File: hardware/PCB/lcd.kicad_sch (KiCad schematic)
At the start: 0 parts

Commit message: Schematic: Create lcd symbol and add to schematic
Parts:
- added DS1: CH430WQ12A-T, symbol CustomSymbols:Adafruit_TFT_480x272_Touchscreen
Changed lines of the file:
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@@
 	(generator_version "9.0")
 	(paper "A4")
+	(symbol
+		(lib_id "CustomSymbols:Adafruit_TFT_480x272_Touchscreen")
+		(at 177.8 96.52 0)
+		(unit 1)
+		(exclude_from_sim no)
+		(in_bom yes)
+		(on_board yes)
+		(dnp no)
+		(fields_autoplaced yes)
+		(property "Reference" "DS1"
+			(at 186.055 94.0378 0)
+			(effects
+				(font
+					(size 1.27 1.27)
+				)
+				(justify left)
+			)
+		)
+		(property "Value" "CH430WQ12A-T"
+			(at 186.055 96.4621 0)
+			(effects
+				(font
+					(size 1.27 1.27)
+				)
+				(justify left)
+			)
+		)
+		(property "Footprint" ""
+			(at 177.8 96.52 0)
+			(effects
+				(font
+					(size 1.27 1.27)
+				)
+				(hide yes)
+			)
+		)
+		(property "Datasheet" "https://cdn-shop.adafruit.com/product-files/1591/CH430WQ12A-T+display+diagram.png"
+			(at 181.102 152.4 0)
+			(effects
+				(font
+					(size 1.27 1.27)
+				)
+				(hide yes)
+			)
+		)
+		(property "Description" ""
+			(at 177.8 96.52 0)
+			(effects
+				(font
+					(size 1.27 1.27)
+				)
+				(hide yes)
+			)
+		)
+		(pin "8"
+		)
+		(pin "22"
+		)
+		(pin "24"
+		)
+		(pin "26"
+		)
+		(pin "9"
+		)
+		(pin "29"
+		)
+		(pin "31"
+		)
+		(pin "5"
+		)
+		(pin "12"
+		)
+		(pin "14"
+		)
+		(pin "19"
+		)
+		(pin "15"
+		)
+		(pin "3"
+		)
+		(pin "21"
+		)
+		(pin "11"
+		)
+		(pin "13"
+		)
+		(pin "4"
+		)
+		(pin "10"
+		)
+		(pin "18"
+		)
+		(pin "1"
+		)
+		(pin "6"
+		)
+		(pin "16"
+		)
+		(pin "17"
+		)
+		(pin "2"
+		)
+		(pin "7"
+		)
+		(pin "20"
+		)
+		(pin "23"
+		)
+		(pin "25"
+		)
+		(pin "27"
+		)
+		(pin "28"
+		)
+		(pin "30"
+		)
+		(pin "33"
+		)
+		(pin "38"
+		)
+		(pin "32"
+		)
+		(pin "34"
+		)
+		(pin "35"
+		)
+		(pin "40"
+		)
+		(pin "37"
+		)
+		(pin "39"
+		)
+		(pin "36"
+		)
+		(instances
+			(project ""
+				(path "/2826ff7c-9767-4078-8ea2-1cd3a432abf3/e982bc10-c57a-42ac-b92d-a536dd69a0fd"
+					(reference "DS1")
+					(unit 1)
+				)
+			)
+		)
+	)
 )

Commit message: Missing changes in last commit
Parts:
- added U1: TSC2013QRSARQ1, Package_DFN_QFN:Texas_RSA_VQFN-16-1EP_4x4mm_P0.65mm_EP2.7x2.7mm, symbol CustomSymbols:TSC2013QRSARQ1
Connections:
- net at DS1.37 (XR): now also U1.11 (X+)
- net at DS1.38 (YD): now also U1.12 (Y+)
- net at DS1.39 (XL): now also U1.13 (X-)
- net at DS1.40 (YU): now also U1.14 (Y-)
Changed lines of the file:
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@@
 	(generator_version "9.0")
 	(paper "A4")
+	(wire
+		(pts
+			(xy 127 137.16) (xy 175.26 137.16)
+		)
+		(stroke
+			(width 0)
+			(type default)
+		)
+	)
+	(wire
+		(pts
+			(xy 127 144.78) (xy 175.26 144.78)
+		)
+		(stroke
+			(width 0)
+			(type default)
+		)
+	)
+	(wire
+		(pts
+			(xy 127 142.24) (xy 175.26 142.24)
+		)
+		(stroke
+			(width 0)
+			(type default)
+		)
+	)
+	(wire
+		(pts
+			(xy 127 139.7) (xy 175.26 139.7)
+		)
+		(stroke
+			(width 0)
+			(type default)
+		)
+	)
+	(symbol
+		(lib_id "CustomSymbols:TSC2013QRSARQ1")
+		(at 109.22 193.04 0)
+		(unit 1)
+		(exclude_from_sim no)
+		(in_bom yes)
+		(on_board yes)
+		(dnp no)
+		(fields_autoplaced yes)
+		(property "Reference" "U1"
+			(at 111.3633 124.46 0)
+			(effects
+				(font
+					(size 1.27 1.27)
+				)
+				(justify left)
+			)
+		)
+		(property "Value" "TSC2013QRSARQ1"
+			(at 111.3633 127 0)
+			(effects
+				(font
+					(size 1.27 1.27)
+				)
+				(justify left)
+			)
+		)
+		(property "Footprint" "Package_DFN_QFN:Texas_RSA_VQFN-16-1EP_4x4mm_P0.65mm_EP2.7x2.7mm"
+			(at 109.22 193.04 0)
+			(effects
+				(font
+					(size 1.27 1.27)
+				)
+				(hide yes)
+			)
+		)
+		(property "Datasheet" "https://www.ti.com/lit/ds/symlink/tsc2013-q1.pdf?HQS=dis-dk-null-digikeymode-dsf-pf-null-wwe&ts=1768864921231&ref_url=https%253A%252F%252Fwww.ti.com%252Fgeneral%252Fdocs%252Fsuppproductinfo.tsp%253FdistId%253D10%2526gotoUrl%253Dhttps%253A%252F%252Fwww.ti.com%252Flit%252Fgpn%252Ftsc2013-q1"
+			(at 109.22 193.04 0)
+			(effects
+				(font
+					(size 1.27 1.27)
+				)
+				(hide yes)
+			)
+		)
+		(property "Description" "Resistive Touchscreen Driver IC"
+			(at 109.22 193.04 0)
+			(effects
+				(font
+					(size 1.27 1.27)
+				)
+				(hide yes)
+			)
+		)
+		(pin "16"
+		)
+		(pin "3"
+		)
+		(pin "5"
+		)
+		(pin "1"
+		)
+		(pin "7"
+		)
+		(pin "6"
+		)
+		(pin "2"
+		)
+		(pin "10"
+		)
+		(pin "4"
+		)
+		(pin "13"
+		)
+		(pin "8"
+		)
+		(pin "12"
+		)
+		(pin "14"
+		)
+		(pin "15"
+		)
+		(pin "9"
+		)
+		(pin "11"
+		)
+		(instances
+			(project ""
+				(path "/2826ff7c-9767-4078-8ea2-1cd3a432abf3/e982bc10-c57a-42ac-b92d-a536dd69a0fd"
+					(reference "U1")
+					(unit 1)
+				)
+			)
+		)
+	)
 	(symbol
 		(lib_id "CustomSymbols:Adafruit_TFT_480x272_Touchscreen")

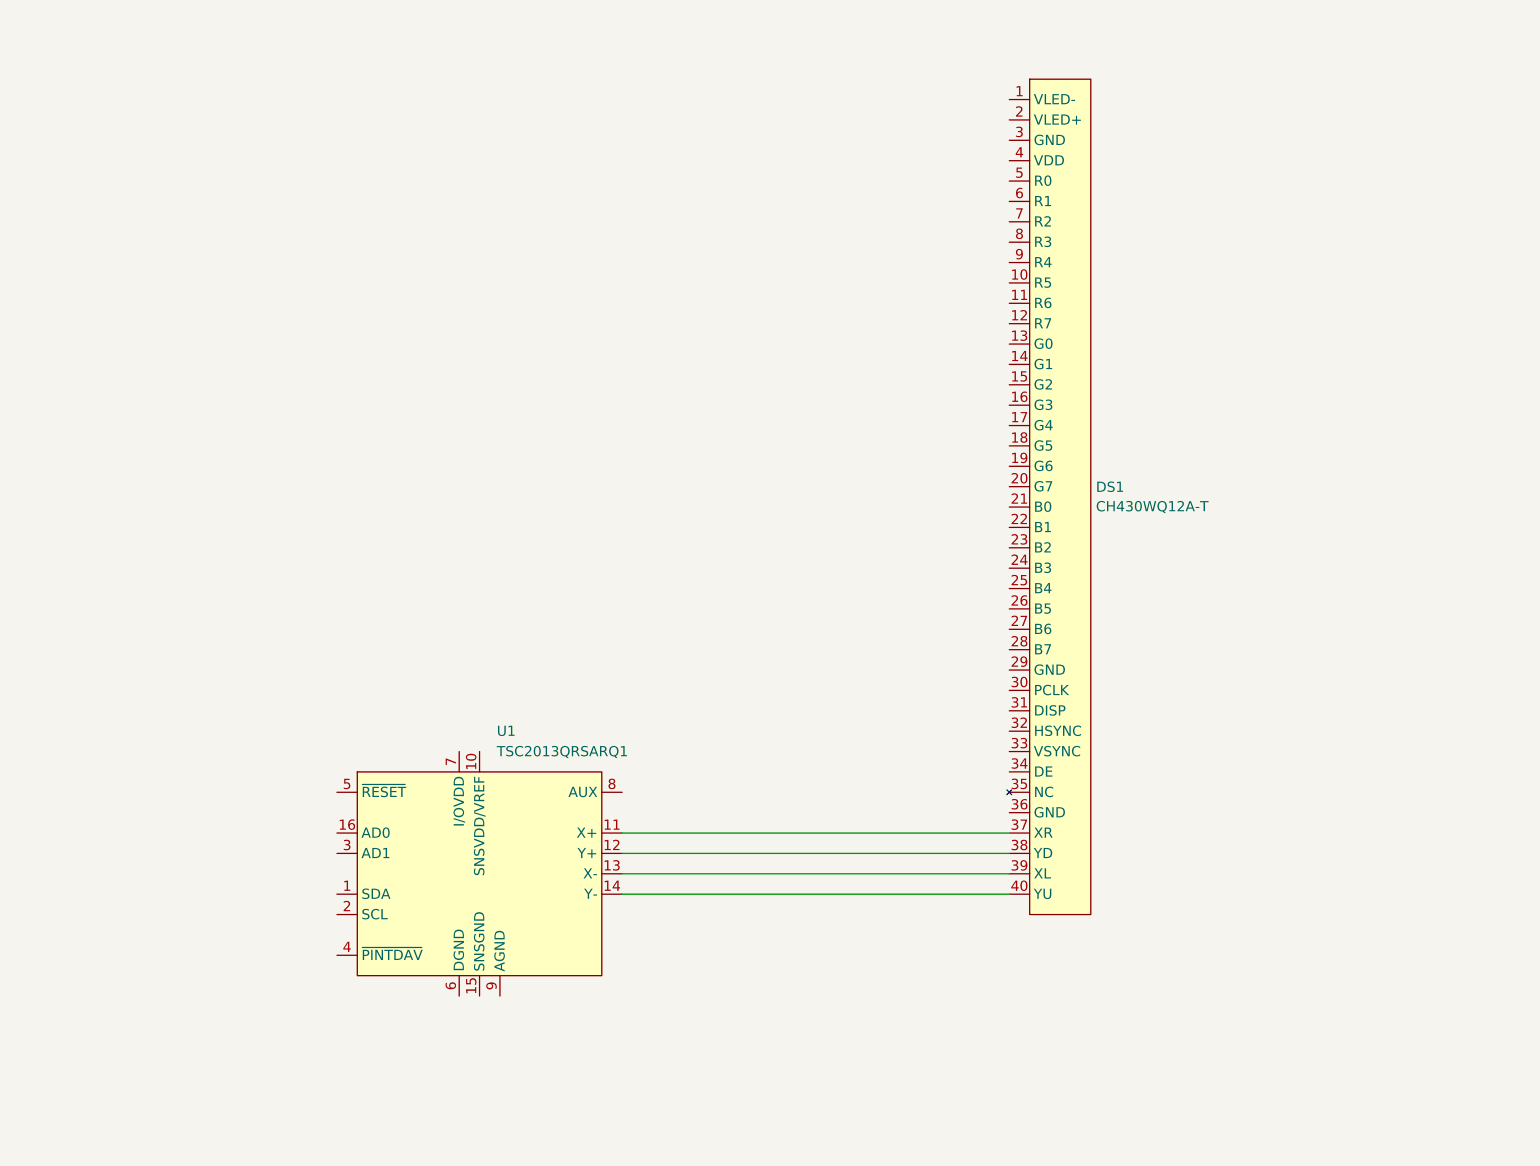
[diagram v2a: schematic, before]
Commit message: LCD: Add in backlight driver, finish wiring
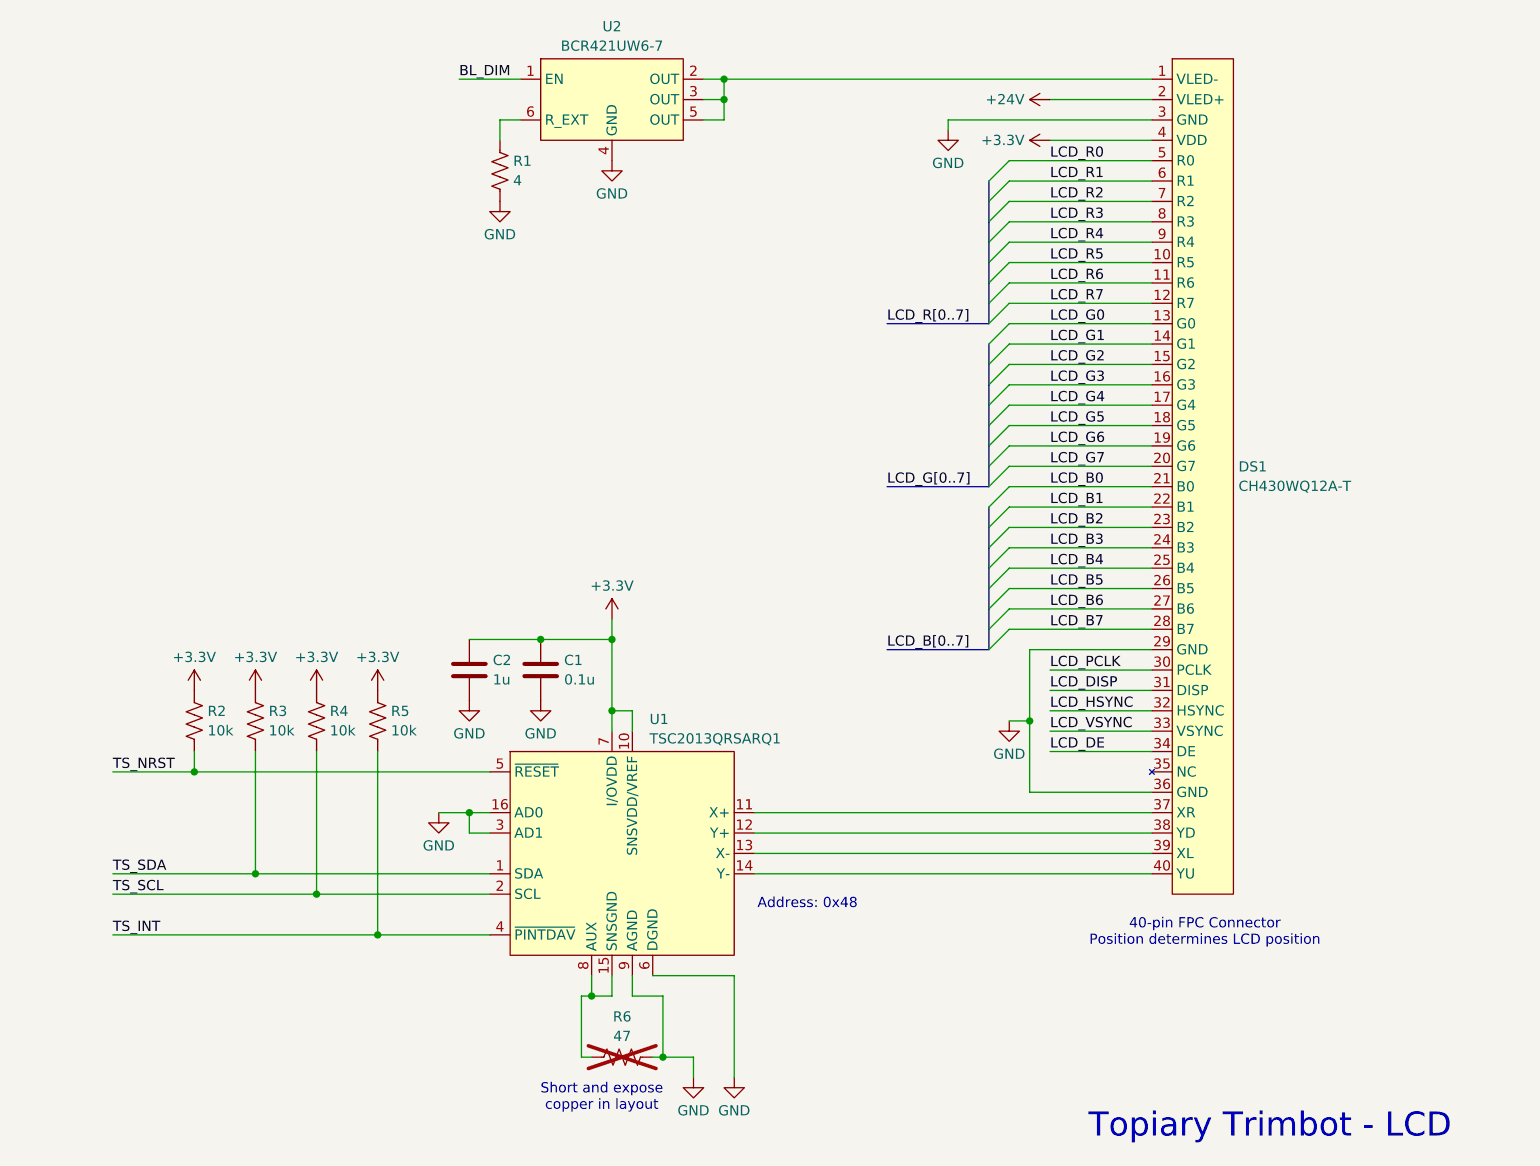
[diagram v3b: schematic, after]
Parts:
- added C1: 0.1u, symbol Device:C
- added C2: 1u, symbol Device:C
- added R1: 4, symbol Device:R_US
- added R2, R3, R4, R5: 10k, symbol Device:R_US
- added R6: 47, Resistor_SMD:R_0805_2012Metric_Pad1.20x1.40mm_HandSolder, symbol Device:R_US
- added U2: BCR421UW6-7, Package_TO_SOT_SMD:SOT-23-6_Handsoldering, symbol CustomSymbols:BCR421UW6-7
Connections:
- net TS_SDA: now reaches U1.1 (SDA)
- net TS_SDA: now also R3.2
- net +3.3V: now reaches U1.10 (SNSVDD/VREF)
- net +3.3V: now also DS1.4 (VDD), U1.7 (I/OVDD), C1.1, C2.1, R2.1, R3.1, R4.1, R5.1
- net at U1.15 (SNSGND): now also U1.8 (AUX), R6.1
- net GND: now reaches U1.16 (AD0)
- net GND: now also DS1.29 (GND), DS1.3 (GND), DS1.36 (GND), U1.3 (AD1), U1.6 (DGND), U1.9 (AGND), C1.2, C2.2, R1.2, R6.2, U2.4 (GND)
- net TS_SCL: now reaches U1.2 (SCL)
- net TS_SCL: now also R4.2
- net TS_INT: now reaches U1.4 (~{PINTDAV})
- net TS_INT: now also R5.2
- net TS_NRST: now reaches U1.5 (~{RESET})
- net TS_NRST: now also R2.2
- net at DS1.1 (VLED-): now also U2.2 (OUT), U2.3 (OUT), U2.5 (OUT)
- net LCD_R5: now reaches DS1.10 (R5)
- net LCD_R6: now reaches DS1.11 (R6)
- net LCD_R7: now reaches DS1.12 (R7)
- net LCD_G0: now reaches DS1.13 (G0)
- net LCD_G1: now reaches DS1.14 (G1)
- net LCD_G2: now reaches DS1.15 (G2)
- net LCD_G3: now reaches DS1.16 (G3)
- net LCD_G4: now reaches DS1.17 (G4)
- net LCD_G5: now reaches DS1.18 (G5)
- net LCD_G6: now reaches DS1.19 (G6)
- net +24V: now reaches DS1.2 (VLED+)
- net LCD_G7: now reaches DS1.20 (G7)
- net LCD_B0: now reaches DS1.21 (B0)
- net LCD_B1: now reaches DS1.22 (B1)
- net LCD_B2: now reaches DS1.23 (B2)
- net LCD_B3: now reaches DS1.24 (B3)
- net LCD_B4: now reaches DS1.25 (B4)
- net LCD_B5: now reaches DS1.26 (B5)
- net LCD_B6: now reaches DS1.27 (B6)
- net LCD_B7: now reaches DS1.28 (B7)
- net LCD_PCLK: now reaches DS1.30 (PCLK)
- net LCD_DISP: now reaches DS1.31 (DISP)
- net LCD_HSYNC: now reaches DS1.32 (HSYNC)
- net LCD_VSYNC: now reaches DS1.33 (VSYNC)
- net LCD_DE: now reaches DS1.34 (DE)
- net LCD_R0: now reaches DS1.5 (R0)
- net LCD_R1: now reaches DS1.6 (R1)
- net LCD_R2: now reaches DS1.7 (R2)
- net LCD_R3: now reaches DS1.8 (R3)
- net LCD_R4: now reaches DS1.9 (R4)
- new net: R1.1, U2.6 (R_EXT)
- new net BL_DIM: U2.1 (EN)
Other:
- note added: "40-pin FPC Connector Position determines LCD position"
- note added: "Address: 0x48"
- note added: "Short and expose copper in layout"
- note added: "Topiary Trimbot - LCD"
- moved on the sheet: DS1

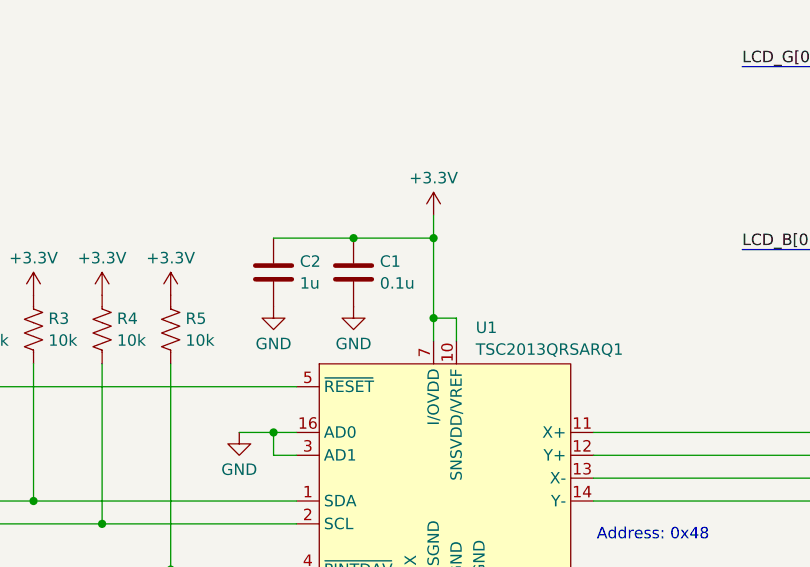
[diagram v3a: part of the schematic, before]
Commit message: Schematic: Symbols, wiring for storage
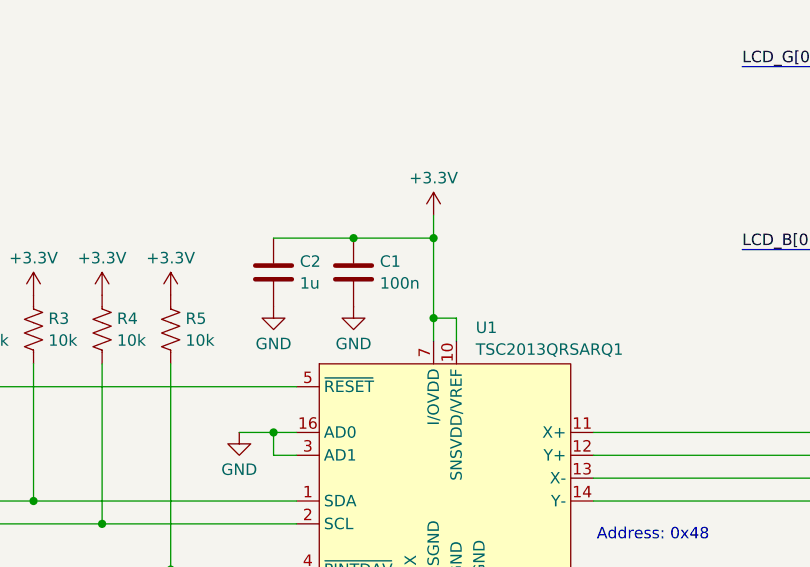
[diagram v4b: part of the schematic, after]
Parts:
- C1: value 0.1u -> 100n
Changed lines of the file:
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@@
 			)
 		)
-		(property "Value" "0.1u"
+		(property "Value" "100n"
 			(at 119.761 118.0521 0)
 			(effects
